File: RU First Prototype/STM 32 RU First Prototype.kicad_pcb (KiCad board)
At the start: 2 copper layers, 81 parts, among them J1 Conn_01x02, J10 Conn_01x02_Pin, J11 Conn_01x02_Pin, J12 1776113-2, J2 USB_C_Receptacle, J3 Conn_01x02_Pin, J4 Conn_01x04, J5 Conn_01x02_Pin, J6 1776113-2, J7 1776113-2, J8 1776113-2, J9 Conn_01x02_Pin, Q1 SISA96DN-T1, Q2 SISA96DN-T1, Q3 SISA96DN-T1, Q4 SISA96DN-T1, SW1 SW_SPDT, U1 STM32F412RGTx, U2 AMS1117-3.3, U3 MS5611, U4 KX134-1211, U5 W25Q16JVSS, U6 TCAN330, U7 TCAN330, Y1 Crystal_8Mhz

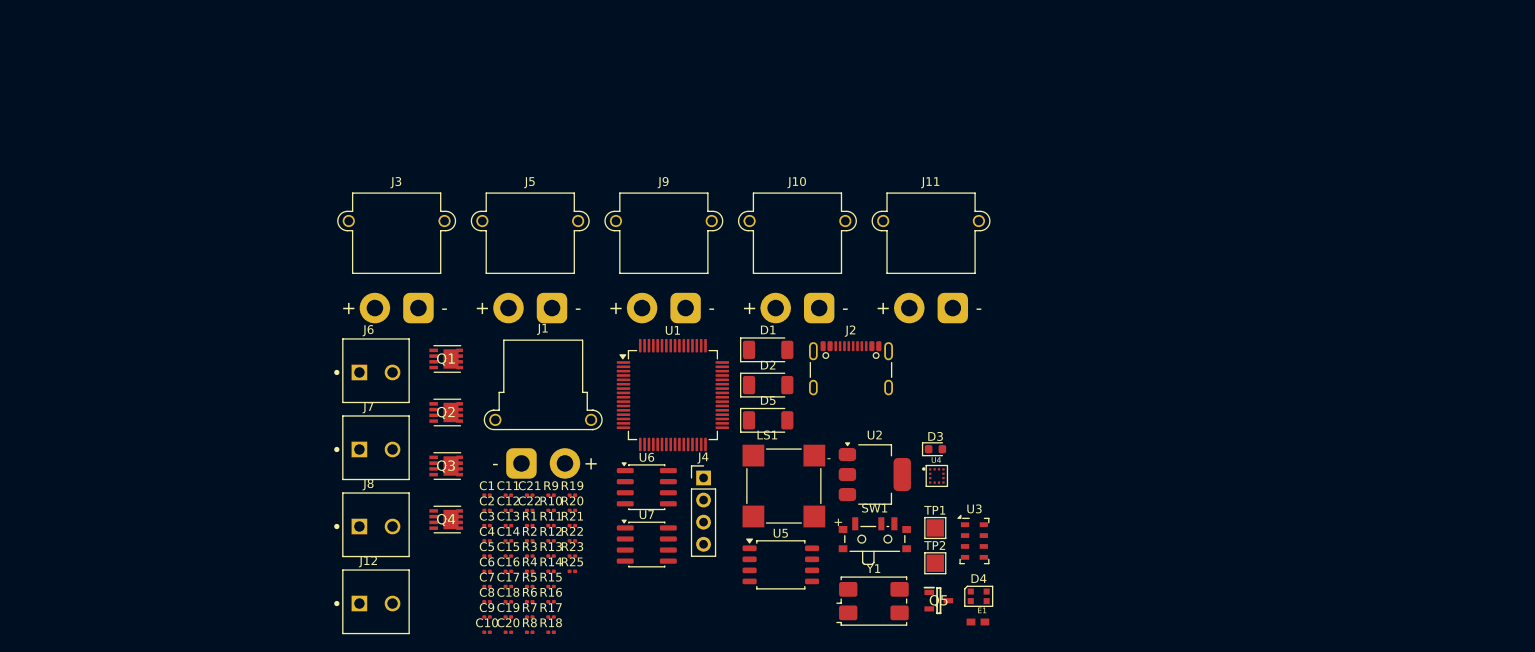
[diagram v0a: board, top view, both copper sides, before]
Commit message: Added 4 layer parameters
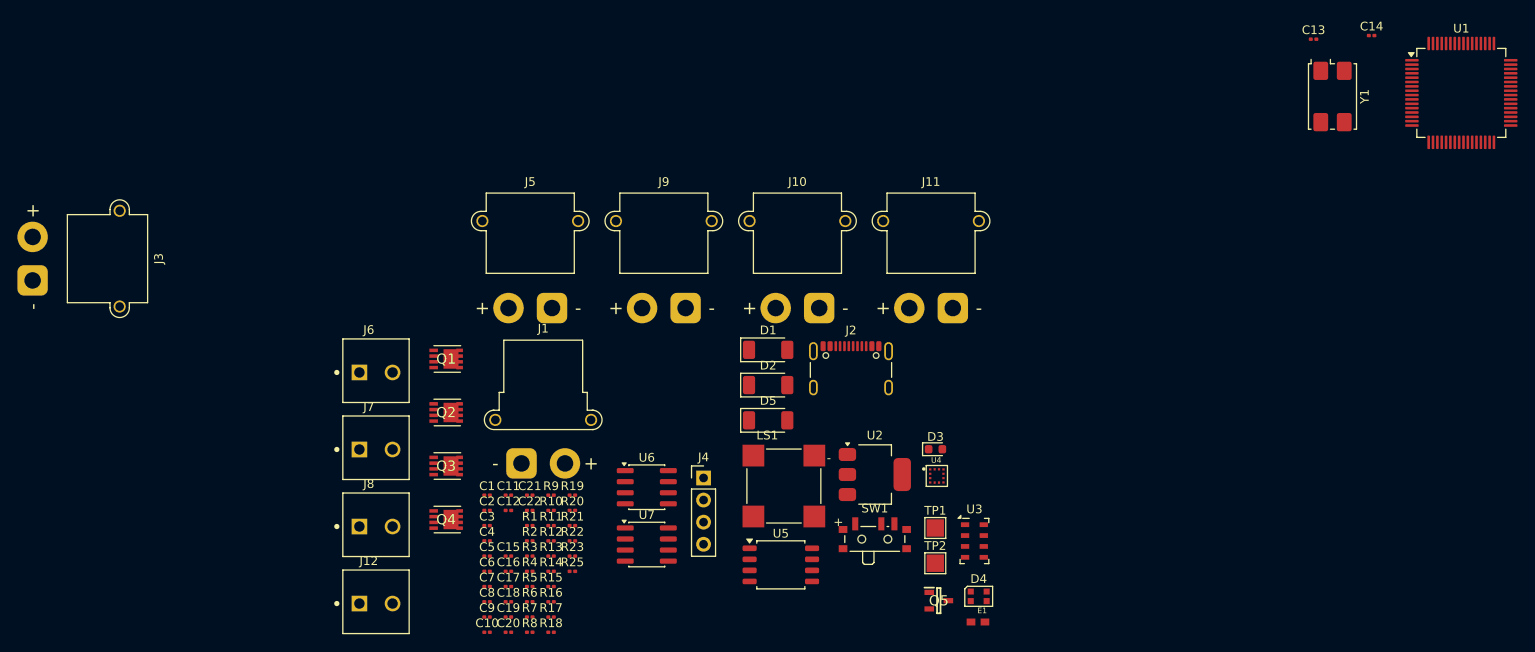
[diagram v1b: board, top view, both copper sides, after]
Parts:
- moved C14 114.9 mm to (230.6, 55.3)
- moved C13 108.1 mm to (223.9, 55.7)
- moved U1 97.0 mm to (240.9, 61.9)
- moved Y1 78.3 mm to (226.1, 62.3), turned to -90 degrees
- moved J3 44.4 mm to (76.7, 83.4), turned to -90 degrees
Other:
- copper layers 2 -> 4

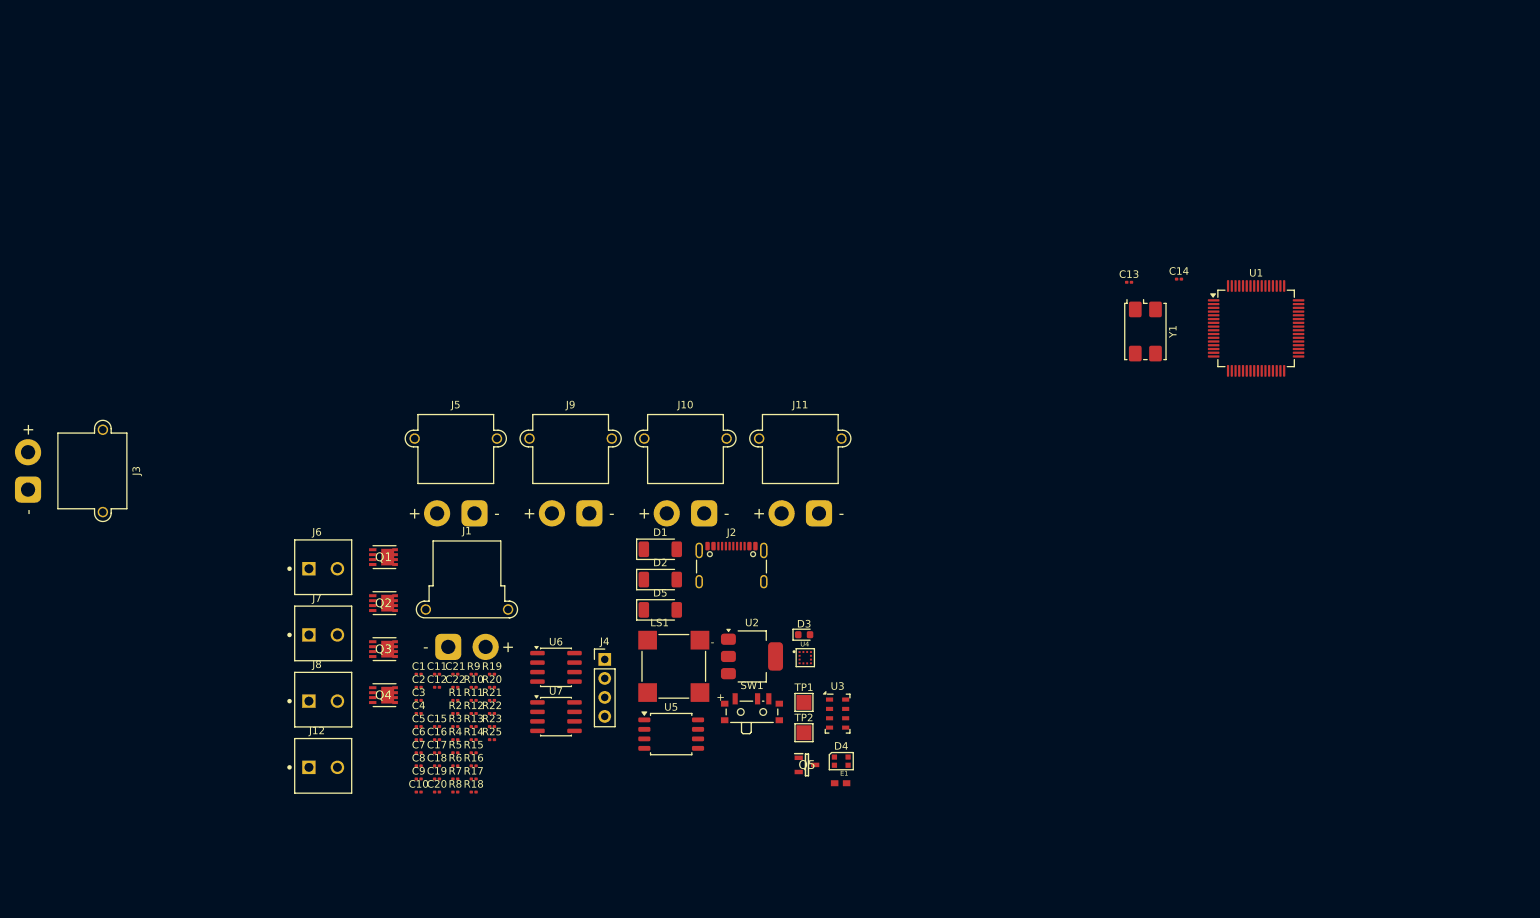
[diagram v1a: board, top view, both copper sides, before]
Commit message: Intermediate circuits of CAN, USB left, Spatial arrangement left
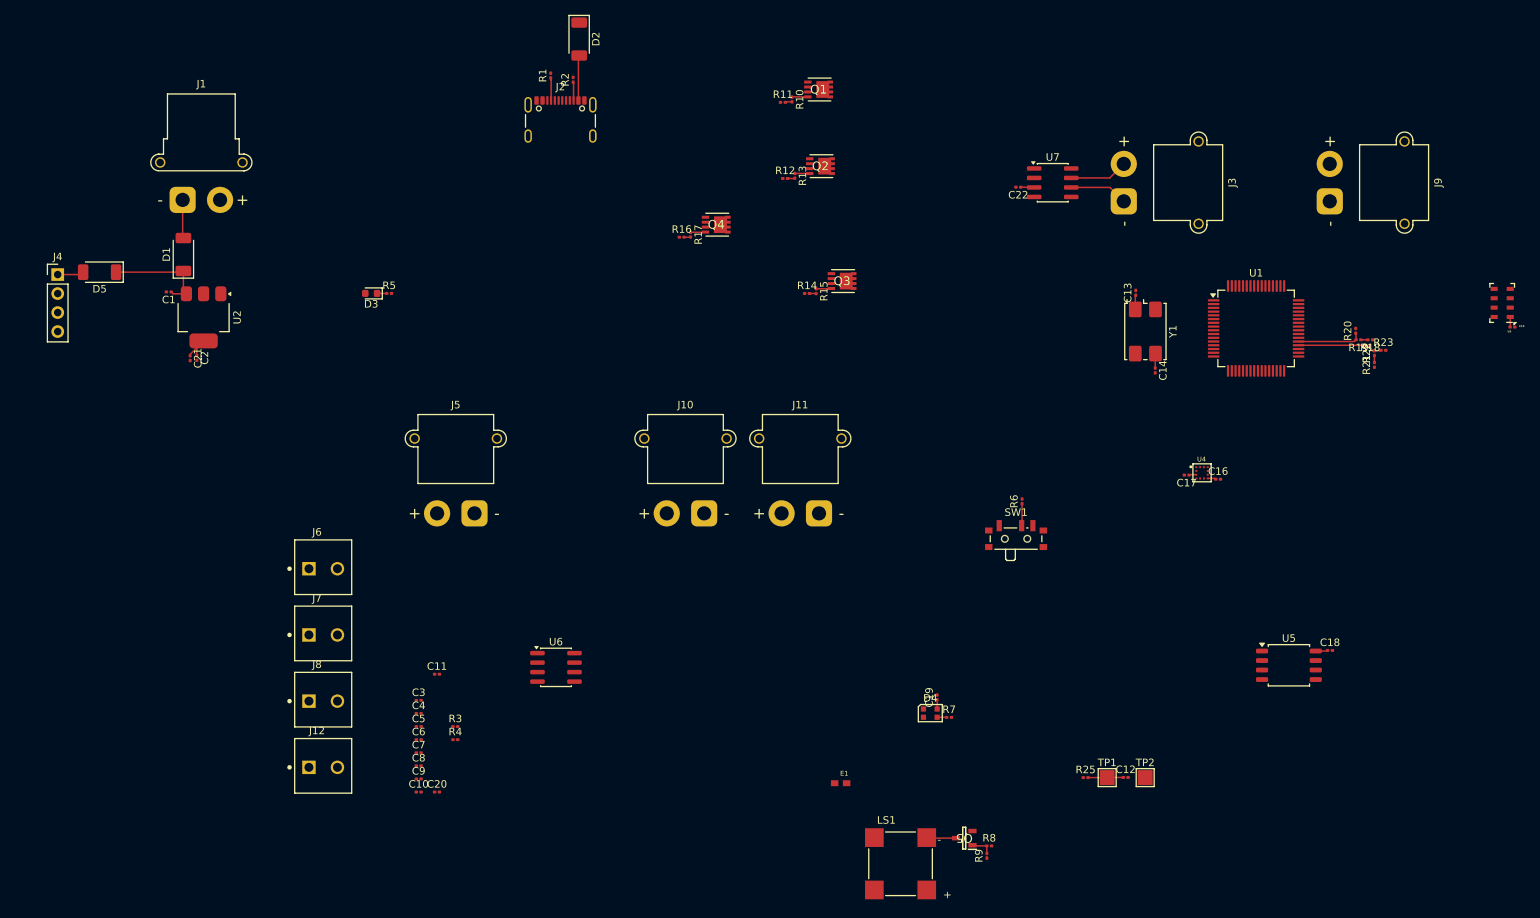
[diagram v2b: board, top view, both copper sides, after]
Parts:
- moved C15 153.4 mm to (275.2, 61.7)
- moved J3 151.4 mm to (223.2, 44.9)
- moved R18 134.2 mm to (256.1, 63.4), turned to 180 degrees
- moved R23 129.3 mm to (257.9, 64.8)
- moved R22 127.4 mm to (256.7, 65.2), turned to 90 degrees
- moved R21 126.2 mm to (256.7, 66.7), turned to 90 degrees
- moved R20 124.9 mm to (254.2, 62.2), turned to 90 degrees
- moved R19 124.1 mm to (254.6, 63.4), turned to 180 degrees
- moved C18 120.4 mm to (250.8, 104.9)
- moved C16 110.1 mm to (235.8, 82.0)
- moved J9 107.4 mm to (250.7, 44.9), turned to -90 degrees
- moved C17 106.9 mm to (231.6, 81.5), turned to 180 degrees
- moved U3 104.4 mm to (273.8, 58.5), turned to 180 degrees
- moved C22 100.7 mm to (209.1, 43.0), turned to 180 degrees
- moved U7 97.5 mm to (213.7, 42.4)
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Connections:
- J3 pad 1: /CAN_H2 -> /CAN_L2
- J9 pad 1: /CAN_H2 -> /CAN_L2
- U7 pad 6: /CAN_H2 -> /CAN_L2
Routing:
- net /V_IN: track 0.00 -> 14.4 mm
- net +3V3: track 0.00 -> 13.2 mm
- net /PB15: track 0.00 -> 11.3 mm
- net /PC6: track 0.00 -> 8.68 mm
- net /CAN_H2: track 0.00 -> 7.80 mm
- net /CAN_L2: track 0.00 -> 7.79 mm
- net /V_USB: track 0.00 -> 6.05 mm
- net /V_2S: track 0.00 -> 5.14 mm
- net /NRST: track 0.00 -> 4.73 mm
- net Net-(Q5-D): track 0.00 -> 3.94 mm
- net /SW_VCC: track 0.00 -> 3.53 mm
- net Net-(J2-CC1): track 0.00 -> 3.03 mm
- net Net-(Q5-G): track 0.00 -> 2.97 mm
- net Net-(SW1-B): track 0.00 -> 2.94 mm
- net Net-(J2-CC2): track 0.00 -> 2.47 mm
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
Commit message: Started Laying traces
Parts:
- added C23: 47pf, Capacitor_SMD:C_0201_0603Metric, F.Cu at (111.3, 29.9)
- added C24: 47pf, Capacitor_SMD:C_0201_0603Metric, F.Cu at (118.3, 30.0)
- added C25: 47pf, Capacitor_SMD:C_0201_0603Metric, F.Cu at (115.8, 71.8)
- added C26: 47pf, Capacitor_SMD:C_0201_0603Metric, F.Cu at (112.7, 71.7)
- added C27: 47pf, Capacitor_SMD:C_0201_0603Metric, F.Cu at (150.4, 117.5)
- added C28: 47pf, Capacitor_SMD:C_0201_0603Metric, F.Cu at (150.3, 120.7)
- added C29: 47pf, Capacitor_SMD:C_0201_0603Metric, F.Cu at (194.6, 122.5)
- added C30: 47pf, Capacitor_SMD:C_0201_0603Metric, F.Cu at (195.1, 115.7)
- added C31: 4.7n, Capacitor_SMD:C_0201_0603Metric, F.Cu at (114.5, 79.9)
- added C32: 4.7n, Capacitor_SMD:C_0201_0603Metric, F.Cu at (141.3, 118.1)
- added CR1: ESDCAN02-2BWY, ESDCAN02-2BWY:SOT323-3L_STM, F.Cu at (114.6, 31.4)
- added CR2: ESDCAN02-2BWY, ESDCAN02-2BWY:SOT323-3L_STM, F.Cu at (193.0, 119.0)
- added CR3: ESDCAN02-2BWY, ESDCAN02-2BWY:SOT323-3L_STM, F.Cu at (114.3, 75.1)
- added CR4: ESDCAN02-2BWY, ESDCAN02-2BWY:SOT323-3L_STM, F.Cu at (145.6, 119.0)
- added R24: 60, Resistor_SMD:R_0201_0603Metric, F.Cu at (112.3, 80.5)
- added R26: 60, Resistor_SMD:R_0201_0603Metric, F.Cu at (116.4, 80.5)
- added R27: 60, Resistor_SMD:R_0201_0603Metric, F.Cu at (140.0, 116.4)
- added R28: 60, Resistor_SMD:R_0201_0603Metric, F.Cu at (139.9, 119.9)
- C16, C17, U4: moved to B.Cu
- moved Q1 175.6 mm to (35.5, 126.0)
- moved R10 175.6 mm to (31.8, 127.4)
- moved R11 175.6 mm to (30.6, 127.8)
- moved D2 159.5 mm to (65.0, 157.9)
- moved J2 159.5 mm to (62.5, 169.8)
- moved R1 159.5 mm to (61.2, 162.8)
- moved R2 159.5 mm to (64.2, 163.4)
- moved R15 158.4 mm to (32.1, 107.8)
- moved Q3 158.4 mm to (35.7, 106.4)
- moved R14 158.4 mm to (30.9, 108.1)
- moved Q2 156.8 mm to (36.2, 96.0)
- moved R12 156.8 mm to (31.3, 97.6)
- moved R13 156.8 mm to (32.6, 97.2)
- moved U3 154.6 mm to (122.4, 89.9), turned to -90 degrees
- moved C15 151.9 mm to (125.7, 88.5), turned to 90 degrees
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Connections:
- J10 pad 1: /CAN_H -> /CAN_L
- J10 pad 2: Net-(J10-Pin_2) -> /CAN_H
- J11 pad 1: /CAN_H -> /CAN_L
- J11 pad 2: Net-(J10-Pin_2) -> /CAN_H
- U1 pad 15: /FLASH_IO3 -> /Buzzer_G
- U1 pad 20: /KX_CS -> unconnected-(U1-PA4-Pad20)
- U1 pad 21: /ALT_SCLK -> unconnected-(U1-PA5-Pad21)
- U1 pad 22: /Buzzer_G -> /FLASH_IO0
- U1 pad 23: /mLED -> /FLASH_IO1
- U1 pad 24: /Drogue2 -> /FLASH_IO2
- U1 pad 25: /ALT_CS -> /FLASH_IO3
- U1 pad 29: /KX_SCK -> unconnected-(U1-PB10-Pad29)
- U1 pad 38: unconnected-(U1-PC7-Pad38) -> /KX_SCK
- U1 pad 39: /FLASH_IO2 -> unconnected-(U1-PC8-Pad39)
- U1 pad 40: /FLASH_IO0 -> /mLED
- U1 pad 51: /FLASH_IO1 -> /Drogue2
- U1 pad 55: unconnected-(U1-PB3-Pad55) -> /ALT_SCLK
- U1 pad 59: unconnected-(U1-PB7-Pad59) -> /ALT_CS
- U1 pad 9: unconnected-(U1-PC1-Pad9) -> /KX_CS
- U6 pad 6: Net-(J10-Pin_2) -> /CAN_L
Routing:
- net /CAN_L: track 0.00 -> 69.5 mm
- net /CAN_H: track 0.00 -> 67.5 mm
- net /CAN_L2: track 7.79 -> 69.3 mm
- net /CAN_H2: track 7.80 -> 69.1 mm
- net /FLASH_CS: track 0.00 -> 20.2 mm, vias 0 -> 2
- net /FLASH_IO0: track 0.00 -> 18.0 mm, vias 0 -> 2
- net /FLASH_IO2: track 0.00 -> 15.5 mm, vias 0 -> 2
- net /KX_SCK: track 0.00 -> 14.6 mm, vias 0 -> 1
- net /FLASH_CLK: track 0.00 -> 13.6 mm
- net /OSC_IN: track 1.95 -> 15.0 mm
- net /FLASH_IO3: track 0.00 -> 12.8 mm
- net /FLASH_IO1: track 0.00 -> 12.2 mm
- net /CAN_TX: track 0.00 -> 9.12 mm
- net /V_MAIN: track 0.00 -> 7.90 mm
- net /V_DROGUE2: track 0.00 -> 7.90 mm
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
